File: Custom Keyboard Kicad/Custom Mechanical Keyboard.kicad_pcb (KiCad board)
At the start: 2 copper layers, 327 x 131.8 mm, 332 parts, among them J1 USB_C_Receptacle_USB2.0_16P, J2 Conn_01x04, J3 Conn_01x05, J4 Conn_01x06, J5 Conn_01x07, J6 Conn_01x20_Socket, J7 Conn_01x20_Socket, SW1 SW_SPST, SW10 SW_SPST, SW11 SW_SPST, SW12 SW_SPST, SW13 SW_SPST, SW14 SW_SPST, SW15 SW_SPST, SW16 SW_SPST, SW17 SW_SPST, SW18 SW_SPST, SW19 SW_SPST, SW2 SW_SPST, SW20 SW_SPST, SW21 SW_SPST, SW22 SW_SPST, SW23 SW_SPST, SW24 SW_SPST, SW25 SW_SPST, SW26 SW_SPST, SW27 SW_SPST, SW28 SW_SPST, SW29 SW_SPST, SW3 SW_SPST, SW30 SW_SPST, SW31 SW_SPST, SW32 SW_SPST, SW33 SW_SPST, SW34 SW_SPST, SW35 SW_SPST, SW36 SW_SPST, SW37 SW_SPST, SW38 SW_SPST, SW39 SW_SPST, SW4 SW_SPST, SW40 SW_SPST, SW41 SW_SPST, SW42 SW_SPST, SW43 SW_SPST, SW44 SW_SPST, SW45 SW_SPST, SW46 SW_SPST, SW47 SW_SPST, SW48 SW_SPST, SW49 SW_SPST, SW5 SW_SPST, SW50 SW_SPST, SW51 SW_SPST, SW52 SW_SPST, SW53 SW_SPST, SW54 SW_SPST, SW55 SW_SPST, SW56 SW_SPST, SW57 SW_SPST, SW58 SW_SPST, SW59 SW_SPST, SW6 SW_SPST, SW60 SW_SPST, SW61 SW_SPST, SW62 SW_SPST, SW63 SW_SPST, SW64 SW_SPST, SW65 SW_SPST, SW66 SW_SPST, SW67 SW_SPST, SW68 SW_SPST, SW69 SW_SPST, SW7 SW_SPST, SW70 SW_SPST, SW71 SW_SPST, SW72 SW_SPST, SW73 SW_SPST, SW74 SW_SPST, SW75 SW_SPST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

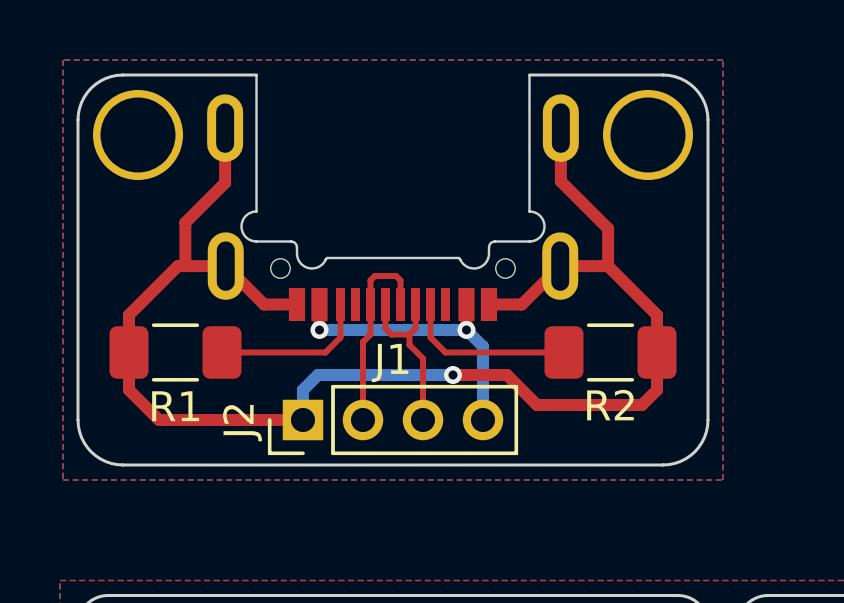
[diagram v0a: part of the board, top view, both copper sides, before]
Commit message: Fix: Changed USB C receptacle to 31M12 instead of 31M14 to fit cheaper assembly requirements
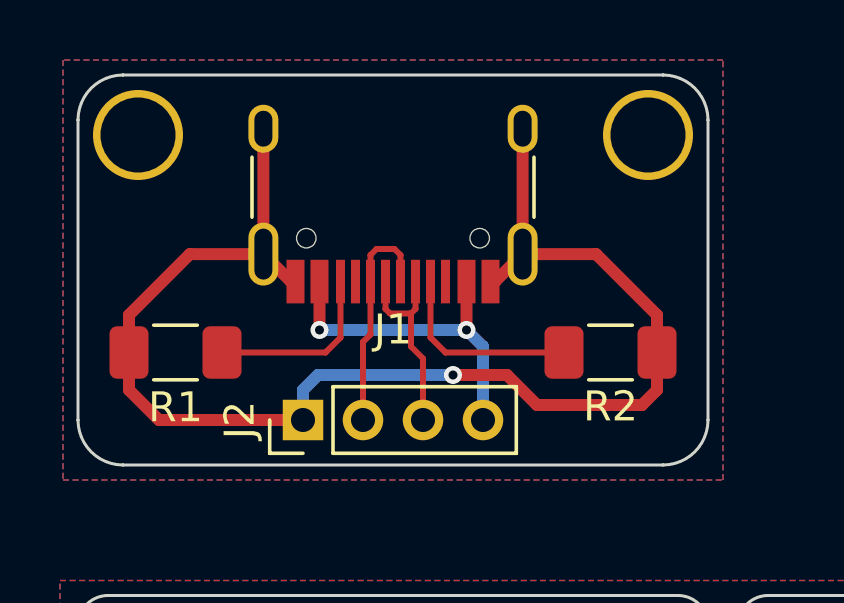
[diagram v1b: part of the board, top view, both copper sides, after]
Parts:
- J1: footprint PCM_marbastlib-various:USB_C_Receptacle_HRO_TYPE-C-31-M-14_(polygon_edge) -> PCM_marbastlib-various:USB_C_Receptacle_HRO_TYPE-C-31-M-12
- moved J1 3.61 mm to (55.0, 33.0)
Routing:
- net USB_GND: track 48.9 -> 46.7 mm
- net /VBUS: track 9.83 -> 11.4 mm
- net /DP: track 6.68 -> 7.65 mm
- net /DM: track 5.80 -> 6.67 mm
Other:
- outline, holes or cut-outs redrawn
